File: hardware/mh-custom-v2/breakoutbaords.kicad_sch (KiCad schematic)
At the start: 8 parts, among them J3 Conn_02x19_Top_Bottom, J4 Conn_02x19_Top_Bottom, U3 AMS1117-3.3

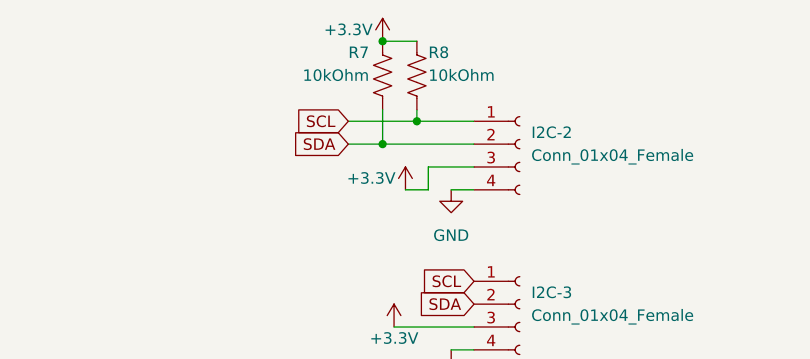
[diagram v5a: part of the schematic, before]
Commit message: after lots of testing, found we need 2.2k resistors for I2C pullup
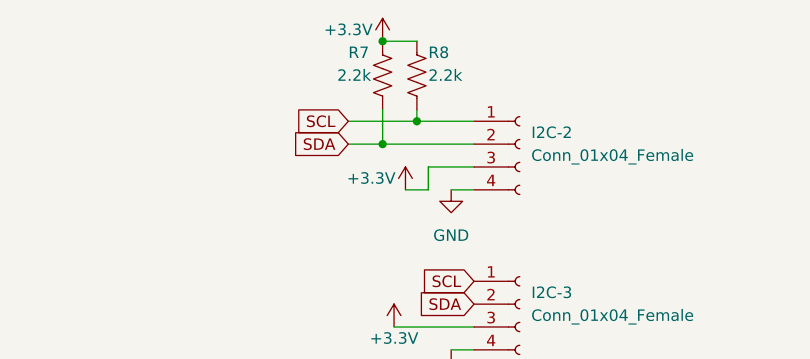
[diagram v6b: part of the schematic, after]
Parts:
- R7, R8: value 10kOhm -> 2.2k; JLCPCB Part # C25804 -> C4190; now in the parts list
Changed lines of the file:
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@@
   )
   (symbol (lib_id "Device:R_US") (at 91.44 39.37 180) (unit 1)
-    (in_bom no) (on_board yes)
+    (in_bom yes) (on_board yes)
     (property "Reference" "R8" (id 0) (at 92.71 36.83 0)
       (effects (font (size 1.27 1.27)) (justify right))
     )
-    (property "Value" "10kOhm" (id 1) (at 92.71 39.37 0)
+    (property "Value" "2.2k" (id 1) (at 92.71 39.37 0)
       (effects (font (size 1.27 1.27)) (justify right))
     )
@@
       (effects (font (size 1.27 1.27)) hide)
     )
-    (property "JLCPCB Part #" "C25804" (id 4) (at 91.44 39.37 0)
+    (property "JLCPCB Part #" "C4190" (id 4) (at 91.44 39.37 0)
       (effects (font (size 1.27 1.27)) hide)
     )
@@
   )
   (symbol (lib_id "Device:R_US") (at 87.63 39.37 180) (unit 1)
-    (in_bom no) (on_board yes)
+    (in_bom yes) (on_board yes)
     (property "Reference" "R7" (id 0) (at 83.82 36.83 0)
       (effects (font (size 1.27 1.27)) (justify right))
     )
-    (property "Value" "10kOhm" (id 1) (at 78.74 39.37 0)
-      (effects (font (size 1.27 1.27)) (justify right))
+    (property "Value" "2.2k" (id 1) (at 86.36 39.37 0)
+      (effects (font (size 1.27 1.27)) (justify left))
     )
     (property "Footprint" "Resistor_SMD:R_0603_1608Metric" (id 2) (at 86.614 39.116 90)
@@
       (effects (font (size 1.27 1.27)) hide)
     )
-    (property "JLCPCB Part #" "C25804" (id 4) (at 87.63 39.37 0)
-      (effects (font (size 1.27 1.27)) hide)
-    )
+    (property "JLCPCB Part #" "C4190" (id 4) (at 87.63 39.37 0)
+      (effects (font (size 1.27 1.27)) hide)
+    )

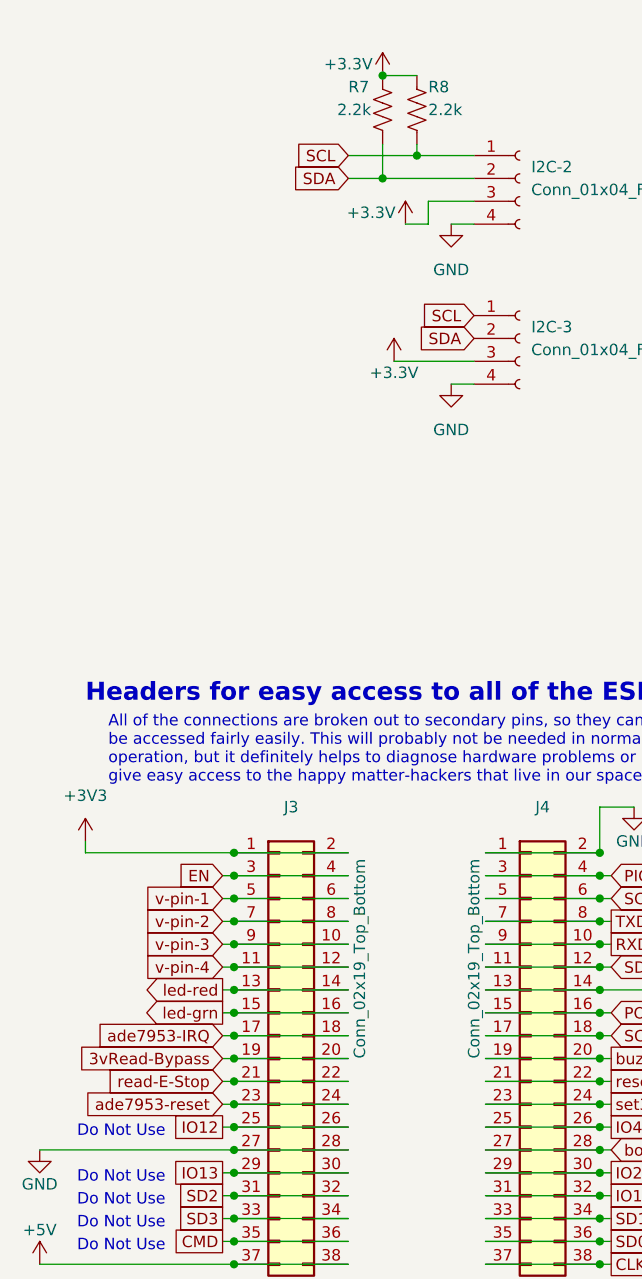
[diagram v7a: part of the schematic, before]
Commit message: b-silkscreen fixed
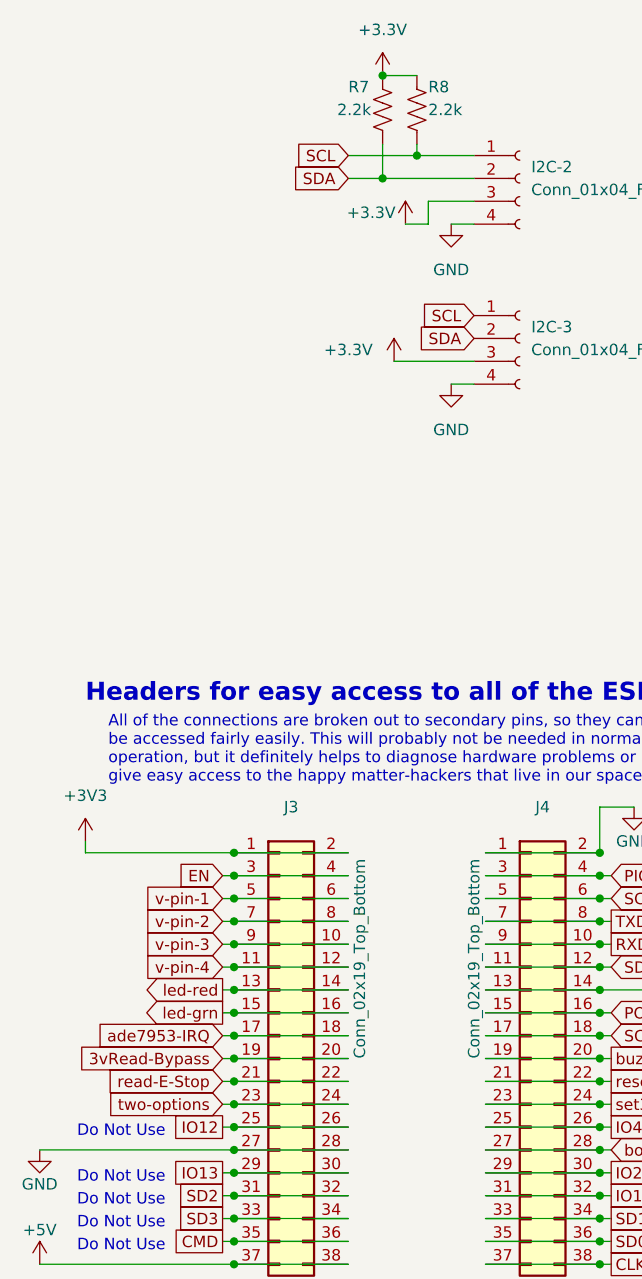
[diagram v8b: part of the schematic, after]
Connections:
- net +3V3: no longer I2C-2.3 (Pin_3), I2C-3.3 (Pin_3), R7.2, R8.2, SPI-1.5 (Pin_5), U3.2 (VO)
- net ade7953-reset renamed two-options
- new net +3.3V: I2C-2.3 (Pin_3), I2C-3.3 (Pin_3), R7.2, R8.2, SPI-1.5 (Pin_5), U3.2 (VO)
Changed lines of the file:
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@@
   (junction (at 111.76 157.48) (diameter 0) (color 0 0 0 0)
   )
+  (junction (at 87.63 35.56) (diameter 0) (color 0 0 0 0)
+  )
   (junction (at 111.76 142.24) (diameter 0) (color 0 0 0 0)
   )
   (junction (at 71.12 162.56) (diameter 0) (color 0 0 0 0)
-  )
-  (junction (at 87.63 35.56) (diameter 0) (color 0 0 0 0)
   )
   (junction (at 71.12 132.08) (diameter 0) (color 0 0 0 0)
@@
     )
   )
-  (global_label "ade7953-reset" (shape input) (at 69.85 149.86 180) (fields_autoplaced)
-    (effects (font (size 1.27 1.27)) (justify right))
-    (property "Intersheet References" "${INTERSHEET_REFS}" (id 0) (at 52.9226 149.7806 0)
+  (global_label "two-options" (shape input) (at 69.85 149.86 180) (fields_autoplaced)
+    (effects (font (size 1.27 1.27)) (justify right))
+    (property "Intersheet References" "${INTERSHEET_REFS}" (id 0) (at 55.7045 149.7806 0)
       (effects (font (size 1.27 1.27)) (justify right) hide)
     )
@@
     (pin "1")
     (pin "2")
-  )
-  (symbol (lib_id "power:+3.3V") (at 88.9 67.31 0) (unit 1)
-    (in_bom yes) (on_board yes)
-    (property "Reference" "#PWR0117" (id 0) (at 88.9 71.12 0)
-      (effects (font (size 1.27 1.27)) hide)
-    )
-    (property "Value" "+3.3V" (id 1) (at 88.9 68.58 0))
-    (property "Footprint" "" (id 2) (at 88.9 67.31 0)
-      (effects (font (size 1.27 1.27)) hide)
-    )
-    (property "Datasheet" "" (id 3) (at 88.9 67.31 0)
-      (effects (font (size 1.27 1.27)) hide)
-    )
-    (pin "1")
   )
   (symbol (lib_id "Connector:Conn_01x06_Female") (at 223.52 85.09 0) (unit 1)
@@
     (pin "1")
   )
+  (symbol (lib_name "+3.3V_1") (lib_id "power:+3.3V") (at 201.93 128.27 0) (unit 1)
+    (in_bom yes) (on_board yes) (fields_autoplaced)
+    (property "Reference" "#PWR0117" (id 0) (at 201.93 132.08 0)
+      (effects (font (size 1.27 1.27)) hide)
+    )
+    (property "Value" "+3.3V" (id 1) (at 201.93 123.19 0))
+    (property "Footprint" "" (id 2) (at 201.93 128.27 0)
+      (effects (font (size 1.27 1.27)) hide)
+    )
+    (property "Datasheet" "" (id 3) (at 201.93 128.27 0)
+      (effects (font (size 1.27 1.27)) hide)
+    )
+    (pin "1")
+  )
   (symbol (lib_id "power:+5V") (at 177.8 127 0) (unit 1)
     (in_bom yes) (on_board yes)
@@
     )
     (property "Datasheet" "" (id 3) (at 177.8 127 0)
-      (effects (font (size 1.27 1.27)) hide)
-    )
-    (pin "1")
-  )
-  (symbol (lib_id "power:+3.3V") (at 214.63 91.44 0) (unit 1)
-    (in_bom yes) (on_board yes)
-    (property "Reference" "#PWR0128" (id 0) (at 214.63 95.25 0)
-      (effects (font (size 1.27 1.27)) hide)
-    )
-    (property "Value" "+3.3V" (id 1) (at 210.82 90.17 0))
-    (property "Footprint" "" (id 2) (at 214.63 91.44 0)
-      (effects (font (size 1.27 1.27)) hide)
-    )
-    (property "Datasheet" "" (id 3) (at 214.63 91.44 0)
       (effects (font (size 1.27 1.27)) hide)
     )
@@
     (pin "2")
     (pin "3")
+  )
+  (symbol (lib_name "+3.3V_1") (lib_id "power:+3.3V") (at 87.63 35.56 0) (unit 1)
+    (in_bom yes) (on_board yes) (fields_autoplaced)
+    (property "Reference" "#PWR0109" (id 0) (at 87.63 39.37 0)
+      (effects (font (size 1.27 1.27)) hide)
+    )
+    (property "Value" "+3.3V" (id 1) (at 87.63 30.48 0))
+    (property "Footprint" "" (id 2) (at 87.63 35.56 0)
+      (effects (font (size 1.27 1.27)) hide)
+    )
+    (property "Datasheet" "" (id 3) (at 87.63 35.56 0)
+      (effects (font (size 1.27 1.27)) hide)
+    )
+    (pin "1")
   )
   (symbol (lib_id "Connector_Generic:Conn_02x19_Odd_Even") (at 104.14 144.78 0) (unit 1)
@@
     (pin "1")
   )
-  (symbol (lib_id "power:+3V3") (at 54.61 120.65 0) (unit 1)
-    (in_bom yes) (on_board yes) (fields_autoplaced)
-    (property "Reference" "#PWR05" (id 0) (at 54.61 124.46 0)
-      (effects (font (size 1.27 1.27)) hide)
-    )
-    (property "Value" "+3V3" (id 1) (at 54.61 115.57 0))
-    (property "Footprint" "" (id 2) (at 54.61 120.65 0)
-      (effects (font (size 1.27 1.27)) hide)
-    )
-    (property "Datasheet" "" (id 3) (at 54.61 120.65 0)
-      (effects (font (size 1.27 1.27)) hide)
-    )
-    (pin "1")
-  )
   (symbol (lib_id "power:GND") (at 115.57 116.84 0) (unit 1)
     (in_bom yes) (on_board yes)
@@
     (pin "4")
   )
-  (symbol (lib_id "power:+3.3V") (at 87.63 35.56 0) (unit 1)
-    (in_bom yes) (on_board yes)
-    (property "Reference" "#PWR0116" (id 0) (at 87.63 39.37 0)
-      (effects (font (size 1.27 1.27)) hide)
-    )
-    (property "Value" "+3.3V" (id 1) (at 83.82 34.29 0))
-    (property "Footprint" "" (id 2) (at 87.63 35.56 0)
-      (effects (font (size 1.27 1.27)) hide)
-    )
-    (property "Datasheet" "" (id 3) (at 87.63 35.56 0)
-      (effects (font (size 1.27 1.27)) hide)
-    )
-    (pin "1")
-  )
-  (symbol (lib_id "power:+3.3V") (at 90.17 52.07 0) (unit 1)
-    (in_bom yes) (on_board yes)
-    (property "Reference" "#PWR0115" (id 0) (at 90.17 55.88 0)
-      (effects (font (size 1.27 1.27)) hide)
-    )
-    (property "Value" "+3.3V" (id 1) (at 86.36 50.8 0))
-    (property "Footprint" "" (id 2) (at 90.17 52.07 0)
-      (effects (font (size 1.27 1.27)) hide)
-    )
-    (property "Datasheet" "" (id 3) (at 90.17 52.07 0)
+  (symbol (lib_name "+3.3V_1") (lib_id "power:+3.3V") (at 214.63 91.44 0) (unit 1)
+    (in_bom yes) (on_board yes)
+    (property "Reference" "#PWR0116" (id 0) (at 214.63 95.25 0)
+      (effects (font (size 1.27 1.27)) hide)
+    )
+    (property "Value" "+3.3V" (id 1) (at 210.82 90.17 0))
+    (property "Footprint" "" (id 2) (at 214.63 91.44 0)
+      (effects (font (size 1.27 1.27)) hide)
+    )
+    (property "Datasheet" "" (id 3) (at 214.63 91.44 0)
       (effects (font (size 1.27 1.27)) hide)
     )
@@
     (pin "9")
   )
-  (symbol (lib_id "power:+3.3V") (at 201.93 128.27 0) (unit 1)
-    (in_bom yes) (on_board yes) (fields_autoplaced)
-    (property "Reference" "#PWR08" (id 0) (at 201.93 132.08 0)
-      (effects (font (size 1.27 1.27)) hide)
-    )
-    (property "Value" "+3.3V" (id 1) (at 201.93 123.19 0))
-    (property "Footprint" "" (id 2) (at 201.93 128.27 0)
-      (effects (font (size 1.27 1.27)) hide)
-    )
-    (property "Datasheet" "" (id 3) (at 201.93 128.27 0)
+  (symbol (lib_name "+3.3V_1") (lib_id "power:+3.3V") (at 90.17 52.07 0) (unit 1)
+    (in_bom yes) (on_board yes)
+    (property "Reference" "#PWR0103" (id 0) (at 90.17 55.88 0)
+      (effects (font (size 1.27 1.27)) hide)
+    )
+    (property "Value" "+3.3V" (id 1) (at 86.36 50.8 0))
+    (property "Footprint" "" (id 2) (at 90.17 52.07 0)
+      (effects (font (size 1.27 1.27)) hide)
+    )
+    (property "Datasheet" "" (id 3) (at 90.17 52.07 0)
       (effects (font (size 1.27 1.27)) hide)
     )
@@
       (effects (font (size 1.27 1.27)) hide)
     )
+    (pin "1")
+  )
+  (symbol (lib_name "+3.3V_1") (lib_id "power:+3.3V") (at 88.9 67.31 0) (unit 1)
+    (in_bom yes) (on_board yes)
+    (property "Reference" "#PWR0115" (id 0) (at 88.9 71.12 0)
+      (effects (font (size 1.27 1.27)) hide)
+    )
+    (property "Value" "+3.3V" (id 1) (at 83.82 66.04 0))
+    (property "Footprint" "" (id 2) (at 88.9 67.31 0)
+      (effects (font (size 1.27 1.27)) hide)
+    )
+    (property "Datasheet" "" (id 3) (at 88.9 67.31 0)
+      (effects (font (size 1.27 1.27)) hide)
+    )
+    (pin "1")
+  )
+  (symbol (lib_id "power:+3V3") (at 54.61 120.65 0) (unit 1)
+    (in_bom yes) (on_board yes) (fields_autoplaced)
+    (property "Reference" "#PWR09" (id 0) (at 54.61 124.46 0)
+      (effects (font (size 1.27 1.27)) hide)
+    )
+    (property "Value" "+3V3" (id 1) (at 54.61 115.57 0))
+    (property "Footprint" "" (id 2) (at 54.61 120.65 0)
+      (effects (font (size 1.27 1.27)) hide)
+    )
+    (property "Datasheet" "" (id 3) (at 54.61 120.65 0)
+      (effects (font (size 1.27 1.27)) hide)
+    )
